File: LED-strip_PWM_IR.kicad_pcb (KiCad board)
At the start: 2 copper layers, 32 x 16 mm, 20 parts, among them IC1 ATTINY85-S, P1 CONN_2, P2 CONN_2, Q1 8MHz, T1 IRLR2905_DPAK, U1 TSOP38238, U2 MCP1804-SOT23-5

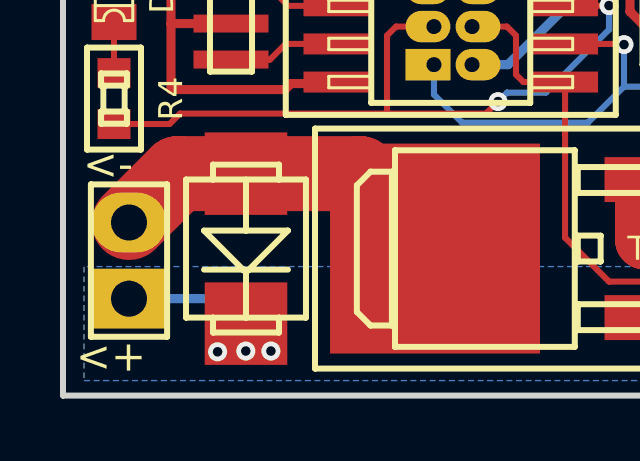
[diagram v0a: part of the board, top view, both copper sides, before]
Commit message: Fixed a brain-fart... Why use a direct trace, if you can use lots of vias?
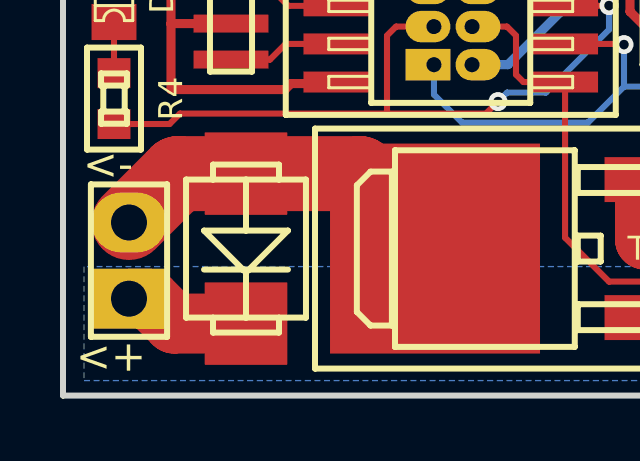
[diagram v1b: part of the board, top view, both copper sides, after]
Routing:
- net /Vin: track 24.6 -> 20.2 mm, vias 4 -> 1
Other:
- board text added: "V0.41 IR PWM controller"
- board text removed: "V0.4 IR PWM controller"
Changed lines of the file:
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@@
     (thickness 1.6002)
     (drawings 19)
-    (tracks 152)
+    (tracks 144)
     (zones 0)
     (modules 20)
@@
   (title_block
     (title LED-strip_PWM_IR)
-    (rev 0.4)
+    (rev 0.41)
     (company "2012 - blog.spitzenpfeil.org")
   )
@@
     (effects (font (size 1 1) (thickness 0.2)))
   )
-  (gr_text "V0.4\nIR PWM controller" (at 91 50.8) (layer B.SilkS)
+  (gr_text "V0.41\nIR PWM controller" (at 91 50.8) (layer B.SilkS)
     (effects (font (size 1.016 1.016) (thickness 0.2032)) (justify mirror))
   )
@@
   (segment (start 79.9 48.6) (end 86.8 48.6) (width 0.2032) (layer Front) (net 4))
   (segment (start 77.7 48.94836) (end 79.55164 48.94836) (width 0.2032) (layer Front) (net 4) (status 10))
+  (segment (start 78.2 54.77) (end 78.87 54.77) (width 2) (layer Front) (net 5))
+  (segment (start 79.69936 55.59936) (end 82.1 55.59936) (width 2) (layer Front) (net 5))
+  (segment (start 78.87 54.77) (end 79.69936 55.59936) (width 2) (layer Front) (net 5))
   (segment (start 102.5 54.5) (end 102.5 48.6) (width 0.3048) (layer Back) (net 5))
   (segment (start 106 54.77) (end 102.77 54.77) (width 0.3048) (layer Back) (net 5) (status 10))
@@
   (segment (start 102.5 48.6) (end 102.5 48.65004) (width 0.3048) (layer Front) (net 5) (status 30))
   (via (at 102.5 48.6) (size 0.635) (layers Front Back) (net 5) (status 30))
-  (segment (start 78.2 54.77) (end 81.2876 54.77) (width 0.3048) (layer Back) (net 5) (status 10))
-  (segment (start 82.0928 55.6006) (end 81.153 56.5404) (width 0.3048) (layer Back) (net 5))
-  (via (at 81.153 56.5404) (size 0.635) (layers Front Back) (net 5) (status 30))
-  (segment (start 81.153 56.5404) (end 81.1784 56.515) (width 0.3048) (layer Front) (net 5) (status 30))
-  (segment (start 81.1784 56.515) (end 82.0928 56.515) (width 0.3048) (layer Front) (net 5) (status 30))
-  (via (at 82.0928 56.515) (size 0.635) (layers Front Back) (net 5) (status 30))
-  (segment (start 82.0928 56.515) (end 82.931 56.515) (width 0.3048) (layer Back) (net 5))
-  (via (at 82.931 56.515) (size 0.635) (layers Front Back) (net 5) (status 30))
-  (segment (start 82.931 56.515) (end 82.1 55.59936) (width 0.3048) (layer Front) (net 5) (status 30))
-  (segment (start 82.1182 55.6006) (end 82.0928 55.6006) (width 0.3048) (layer Back) (net 5))
-  (segment (start 81.2876 54.77) (end 82.1182 55.6006) (width 0.3048) (layer Back) (net 5))
   (segment (start 100.44996 48.20206) (end 102.05202 48.20206) (width 0.3048) (layer Front) (net 5) (status 30))
   (segment (start 102.05202 48.20206) (end 102.5 48.65004) (width 0.3048) (layer Front) (net 5) (status 30))
